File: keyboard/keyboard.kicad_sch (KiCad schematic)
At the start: 0 parts

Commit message: Finished electronic schema of MCU
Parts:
- added C1: 1u, symbol Device:C_Small
- added C2, C3: 22p, symbol Device:C_Small
- added C4, C5, C6, C7: 0.1u, symbol Device:C_Small
- added C8: 10u, symbol Device:C_Small
- added F1: 200m, symbol Device:Polyfuse_Small
- added J1: AVR-ISP-6, symbol Connector:AVR-ISP-6
- added R1, R2: 10k, symbol Device:R_Small_US
- added R3, R4: 22, symbol Device:R_Small_US
- added R5, R6: 5.1k, symbol Device:R_Small_US
- added SW1: ~, symbol SW_SKQG:SW_SKQG
- added U1: ATmega32U4-A, Package_QFP:TQFP-44_10x10mm_P0.8mm, symbol MCU_Microchip_ATmega:ATmega32U4-A
- added U2: PRTR5V0U2X, symbol Random-Keyboard-Parts:PRTR5V0U2X
- added USB1: HRO-TYPE-C-31-M-12, symbol Type-C:HRO-TYPE-C-31-M-12
- added Y1: Crystal_GND24_Small, symbol Device:Crystal_GND24_Small
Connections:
- new net: R1.1, U1.33 (~{HWB}/PE2)
- new net: C1.2, U1.6 (UCAP)
- new net: R4.1, U2.2 (IO1), USB1.6 (DP1), USB1.8 (DP2)
- new net: R5.1, USB1.4 (CC1)
- new net: R3.1, U2.3 (IO2), USB1.5 (DN2), USB1.7 (DN1)
- new net +5V: C4.2, C5.2, C6.2, C7.2, C8.2, F1.2, J1.2 (VCC), R2.1, U1.14 (VCC), U1.2 (UVCC), U1.24 (AVCC), U1.34 (VCC), U1.44 (AVCC), U1.7 (VBUS)
- new net D+: R4.2, U1.4 (D+)
- new net D-: R3.2, U1.3 (D-)
- new net GND: C1.1, C2.1, C3.2, C4.1, C5.1, C6.1, C7.1, C8.1, J1.6 (GND), R1.2, R5.2, R6.2, SW1.2, U1.15 (GND), U1.23 (GND), U1.35 (GND), U1.43 (GND), U1.5 (UGND), U2.1 (GND), USB1.1 (GND), USB1.12 (GND), USB1.13 (SHIELD), Y1.2, Y1.4
- new net MISO: J1.1 (MISO), U1.11 (PB3)
- new net MOSI: J1.4 (MOSI), U1.10 (PB2)
- new net RESET: R2.2, SW1.1, U1.13 (~{RESET})
- new net RST: J1.5 (~{RST})
- new net SCK: J1.3 (SCK), U1.9 (PB1)
- new net VCC: F1.1, R6.1, U2.4 (VCC), USB1.10 (CC2), USB1.11 (VBUS), USB1.2 (VBUS)
- new net XTAL1: C2.2, U1.17 (XTAL1), Y1.1
- new net XTAL2: C3.1, U1.16 (XTAL2), Y1.3
- no-connect marks 0 -> 5

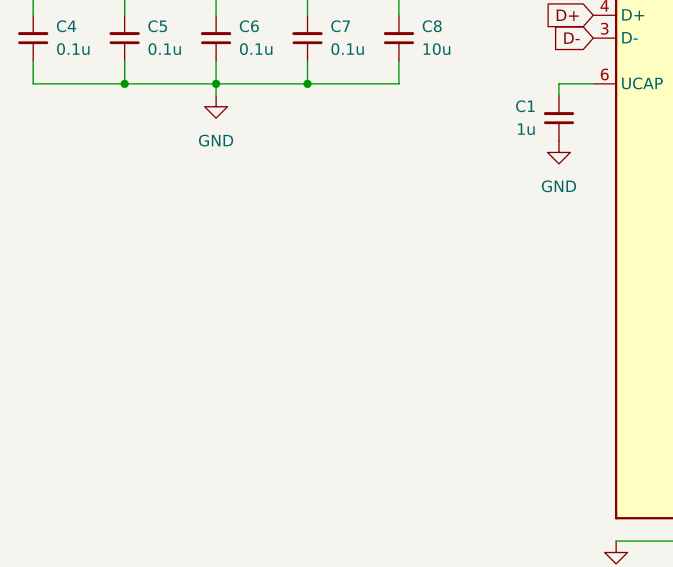
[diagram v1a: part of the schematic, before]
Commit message: Finished electronic schema of matrix
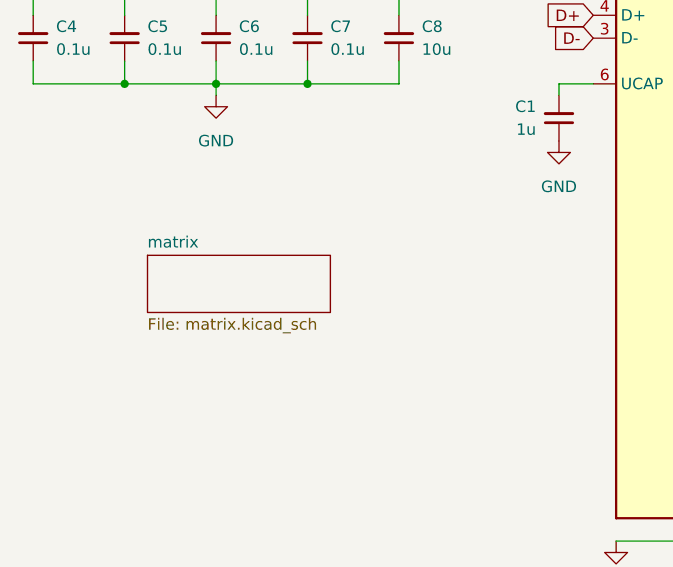
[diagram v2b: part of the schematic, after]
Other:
- added sheet matrix (matrix.kicad_sch)
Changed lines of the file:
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@@
+		)
+	)
+	(sheet
+		(at 74.93 97.79)
+		(size 20.32 6.35)
+		(exclude_from_sim no)
+		(in_bom yes)
+		(on_board yes)
+		(dnp no)
+		(fields_autoplaced yes)
+		(stroke
+			(width 0.1524)
+			(type solid)
+		)
+		(fill
+			(color 0 0 0 0.0000)
+		)
+		(property "Sheetname" "matrix"
+			(at 74.93 97.0784 0)
+			(effects
+				(font
+					(size 1.27 1.27)
+				)
+				(justify left bottom)
+			)
+		)
+		(property "Sheetfile" "matrix.kicad_sch"
+			(at 74.93 104.7246 0)
+			(effects
+				(font
+					(size 1.27 1.27)
+				)
+				(justify left top)
+			)
+		)
+		(instances
+			(project "keyboard"
+				(path "/baf123a7-6ae0-48c9-a702-a751ce843c88"
+					(page "2")
+				)
+			)
 		)
 	)

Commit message: Assigned footprints + fixed errors
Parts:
- C1, C2, C3, C4, C5, C6, C7, C8: footprint (none) -> Capacitor_SMD:C_0805_2012Metric_Pad1.18x1.45mm_HandSolder
- F1: footprint (none) -> Fuse:Fuse_1206_3216Metric_Pad1.42x1.75mm_HandSolder
- J1: footprint (none) -> Random-Keyboard-Parts:Reset_Pretty-Mask
- R1, R2, R3, R4, R5, R6: footprint (none) -> Resistor_SMD:R_0805_2012Metric_Pad1.20x1.40mm_HandSolder
- SW1: footprint (none) -> Button_Switch_Keyboard:SW_Cherry_MX_1.00u_PCB
- U2: footprint (none) -> Random-Keyboard-Parts:SOT143B
- USB1: footprint (none) -> Type-C:HRO-TYPE-C-31-M-12-HandSoldering
- Y1: footprint (none) -> Crystal:Crystal_SMD_3225-4Pin_3.2x2.5mm_HandSoldering
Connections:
- net RST is gone; now on net RESET: J1.5 (~{RST})
- net row0: now reaches U1.1 (PE6)
- net col8: now reaches U1.19 (PD1)
- net col9: now reaches U1.20 (PD2)
- net col10: now reaches U1.21 (PD3)
- net col12: now reaches U1.22 (PD5)
- net col11: now reaches U1.25 (PD4)
- net col13: now reaches U1.26 (PD6)
- net col14: now reaches U1.27 (PD7)
- net col0: now reaches U1.28 (PB4)
- net col1: now reaches U1.29 (PB5)
- net col2: now reaches U1.30 (PB6)
- net col3: now reaches U1.31 (PC6)
- net col4: now reaches U1.32 (PC7)
- net col6: now reaches U1.36 (PF7)
- net col5: now reaches U1.37 (PF6)
- net row1: now reaches U1.38 (PF5)
- net row4: now reaches U1.39 (PF4)
- net row3: now reaches U1.40 (PF1)
- net row2: now reaches U1.41 (PF0)
- net col7: now reaches U1.8 (PB0)

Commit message: Finished keyboard switch layout for PCB
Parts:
- SW1: footprint Button_Switch_Keyboard:SW_Cherry_MX_1.00u_PCB -> MX:MXOnly-1U
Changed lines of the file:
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@@
 			)
 		)
-		(property "Footprint" "Button_Switch_Keyboard:SW_Cherry_MX_1.00u_PCB"
+		(property "Footprint" "MX:MXOnly-1U"
 			(at 240.03 39.37 0)
 			(effects

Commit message: Finished diode layout and changed switch footprints to no-LED
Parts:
- SW1: footprint MX:MXOnly-1U -> MX:MXOnly-1U-NoLED
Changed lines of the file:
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@@
 			)
 		)
-		(property "Footprint" "MX:MXOnly-1U"
+		(property "Footprint" "MX:MXOnly-1U-NoLED"
 			(at 240.03 39.37 0)
 			(effects

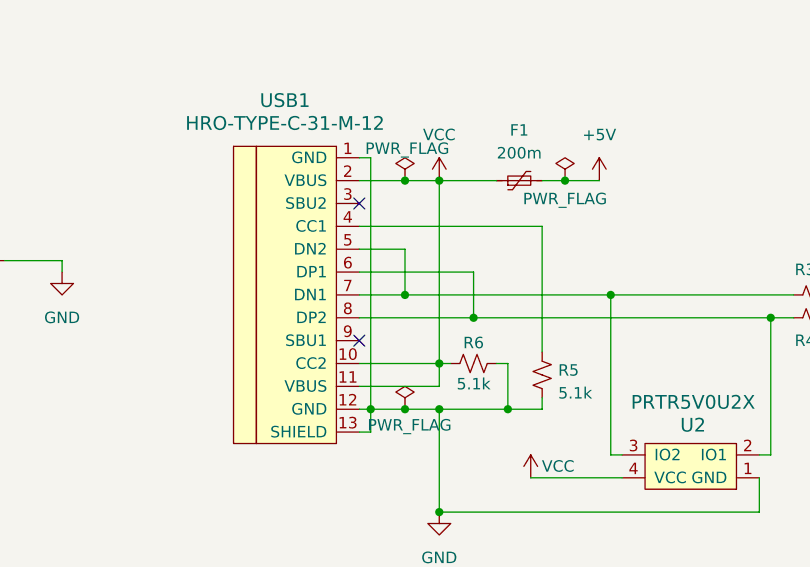
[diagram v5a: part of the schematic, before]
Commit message: Crudely arranged USB-C and MCU footprints and cut PCB edges.
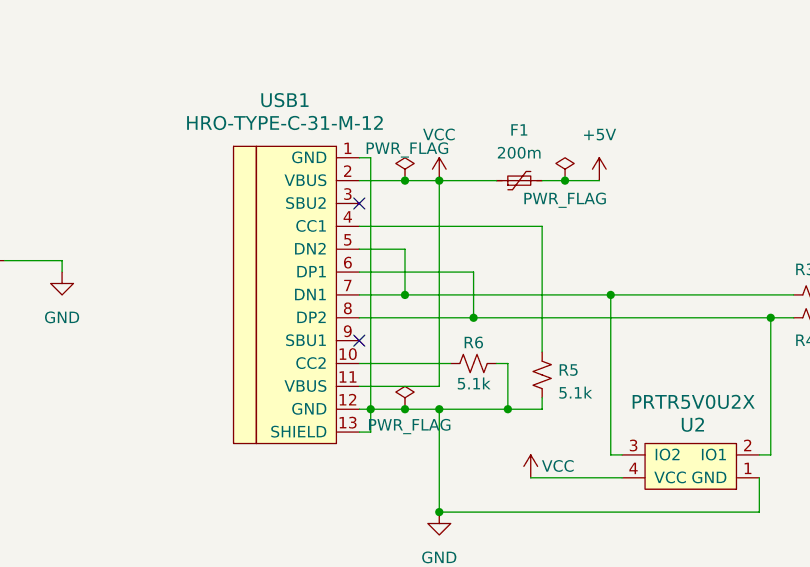
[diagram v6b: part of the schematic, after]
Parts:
- SW1: footprint MX:MXOnly-1U-NoLED -> Button_Switch_SMD:SW_SPST_SKQG_WithStem
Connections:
- net VCC: no longer R6.1, USB1.10 (CC2)
- new net: R6.1, USB1.10 (CC2)
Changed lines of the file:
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@@
 	)
 	(junction
-		(at 213.36 110.49)
-		(diameter 0)
-		(color 0 0 0 0)
-	)
-	(junction
 		(at 92.71 68.58)
 		(diameter 0)
@@
 	(wire
 		(pts
-			(xy 204.47 110.49) (xy 213.36 110.49)
+			(xy 204.47 110.49) (xy 214.63 110.49)
 		)
 		(stroke
@@
 	(wire
 		(pts
-			(xy 213.36 110.49) (xy 214.63 110.49)
-		)
-		(stroke
-			(width 0)
-			(type default)
-		)
-	)
-	(wire
-		(pts
 			(xy 171.45 100.33) (xy 171.45 99.06)
 		)
@@
 	(wire
 		(pts
-			(xy 213.36 90.17) (xy 213.36 110.49)
+			(xy 213.36 90.17) (xy 213.36 113.03)
 		)
 		(stroke
@@
 	(wire
 		(pts
-			(xy 213.36 110.49) (xy 213.36 113.03)
-		)
-		(stroke
-			(width 0)
-			(type default)
-		)
-	)
-	(wire
-		(pts
 			(xy 232.41 102.87) (xy 232.41 120.65)
 		)
@@
 			)
 		)
-		(property "Footprint" "MX:MXOnly-1U-NoLED"
+		(property "Footprint" "Button_Switch_SMD:SW_SPST_SKQG_WithStem"
 			(at 240.03 39.37 0)
 			(effects
